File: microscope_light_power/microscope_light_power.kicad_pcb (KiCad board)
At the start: 2 copper layers, 50 x 40 mm, 36 parts, among them J1 MICROUSB, J2 5V175_out, J3 enable_switch, U1 MCP73871-2AA, U2 TPS61090

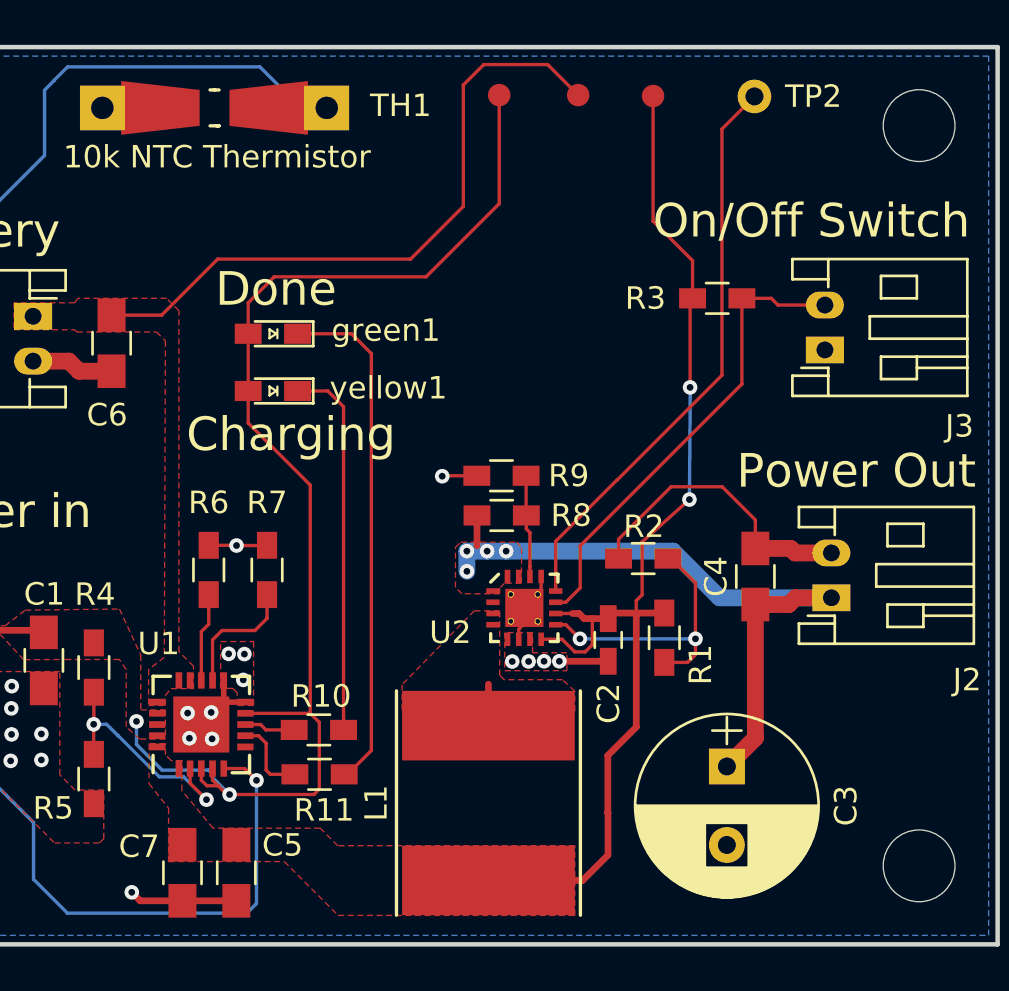
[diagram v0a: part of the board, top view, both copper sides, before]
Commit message: Add more silkscreen labels for clarity
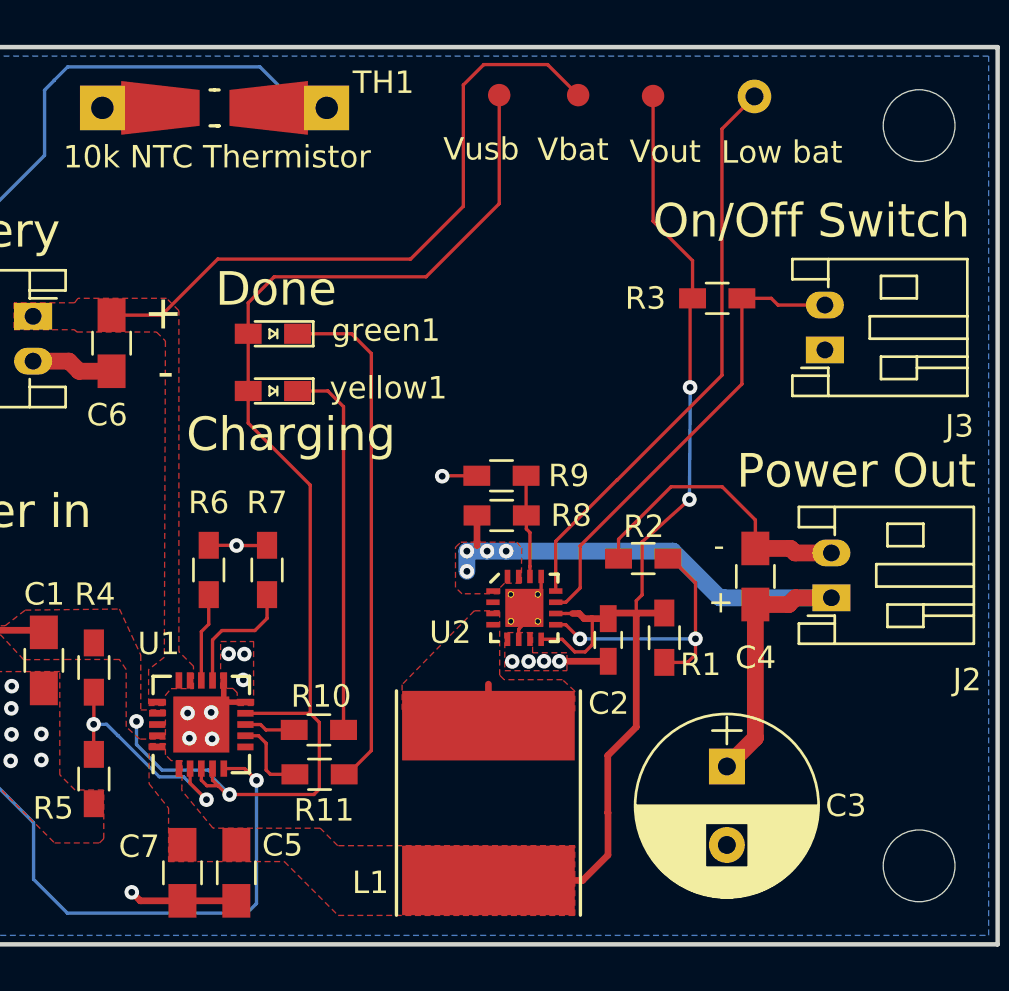
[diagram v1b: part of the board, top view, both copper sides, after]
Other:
- board text added: "+"
- board text added: "-"
- board text added: "5V@1.5A out"
- board text added: "Jon Neal"
- board text added: "Low bat"
- board text added: "USB battery charger with 5V out"
- board text added: "Vbat"
- board text added: "Vout"
- board text added: "Vusb"
- board text added: "github.com/reportingsjr/microscope_light_power"
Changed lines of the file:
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@@
 (general
   (thickness 1.6)
-  (drawings 15)
+  (drawings 27)
   (tracks 234)
   (zones 0)
@@
 (general
   (thickness 1.6)
-  (drawings 15)
+  (drawings 27)
   (tracks 234)
   (zones 0)
@@
     (tags "capacitor 0603")
     (attr smd)
-    (fp_text reference C2 (at 2.83 -0.02 270) (layer F.SilkS)
+    (fp_text reference C2 (at 2.83 -0.02) (layer F.SilkS)
       (effects (font (size 1 1) (thickness 0.15)))
     )
@@
     (fp_line (start 0.8 0.4) (end -0.8 0.4) (layer F.Fab) (width 0.1))
     (fp_line (start -0.8 0.4) (end -0.8 -0.4) (layer F.Fab) (width 0.1))
-    (fp_text user %R (at 2.83 -0.02 270) (layer F.Fab)
+    (fp_text user %R (at 2.83 -0.02) (layer F.Fab)
       (effects (font (size 1 1) (thickness 0.15)))
     )
@@
     (tags "capacitor 0805")
     (attr smd)
-    (fp_text reference C4 (at 0 -1.75 90) (layer F.SilkS)
+    (fp_text reference C4 (at -3.62 0.01) (layer F.SilkS)
       (effects (font (size 1 1) (thickness 0.15)))
     )
@@
       (effects (font (size 1 1) (thickness 0.15)))
     )
-    (fp_text user %R (at 0 -1.75 90) (layer F.Fab)
+    (fp_text user %R (at -3.62 0.01 180) (layer F.Fab)
       (effects (font (size 1 1) (thickness 0.15)))
     )
@@
     (descr "CP, Radial series, Radial, pin pitch=3.50mm, , diameter=8mm, Electrolytic Capacitor")
     (tags "CP Radial series Radial pin pitch 3.50mm  diameter 8mm Electrolytic Capacitor")
-    (fp_text reference C3 (at 1.75 -5.31 270) (layer F.SilkS)
+    (fp_text reference C3 (at 1.75 -5.31) (layer F.SilkS)
       (effects (font (size 1 1) (thickness 0.15)))
     )
@@
     (tags "inductor taiyo-yuden nr smd")
     (attr smd)
-    (fp_text reference L1 (at 0 -5 90) (layer F.SilkS)
+    (fp_text reference L1 (at -3.55 -5.26 180) (layer F.SilkS)
       (effects (font (size 1 1) (thickness 0.15)))
     )
@@
     (tags "Mesurement Point Round Trough Hole 1.5mm Drill 0.8mm")
     (attr virtual)
-    (fp_text reference TP2 (at 2.63 0) (layer F.SilkS)
+    (fp_text reference TP2 (at 2.63 0) (layer F.SilkS) hide
       (effects (font (size 1 1) (thickness 0.15)))
     )
@@
     (tags "resistor 0603")
     (attr smd)
-    (fp_text reference R1 (at 1.2 -1.62 270) (layer F.SilkS)
+    (fp_text reference R1 (at 1.2 -1.62) (layer F.SilkS)
       (effects (font (size 1 1) (thickness 0.15)))
     )
@@
     (descr "Resistor, SMD and THT, universal, 0805 to 1206,RM10,  Hand soldering,")
     (tags "Resistor, SMD and THT, universal, 0805 to 1206, RM10, Hand soldering,")
-    (fp_text reference TH1 (at -8.3 0.1 180) (layer F.SilkS)
+    (fp_text reference TH1 (at -7.53 1.13 180) (layer F.SilkS)
       (effects (font (size 1 1) (thickness 0.15)))
     )
@@
   (module agg:MICROUSB_MOLEX_47589-0001 (layer F.Cu)
     (at 101.5 147.3 270)
-    (fp_text reference J1 (at 5.8 0.6 270) (layer F.Fab)
+    (fp_text reference J1 (at 5.8 0.09) (layer F.Fab)
       (effects (font (size 1 1) (thickness 0.15)))
     )
@@
       (net 1 /Vbat))
   )
+  (gr_text "5V@1.5A out" (at 125.07 149.77) (layer B.SilkS)
+    (effects (font (size 1.5 1.5) (thickness 0.3)) (justify mirror))
+  )
+  (gr_text github.com/reportingsjr/microscope_light_power (at 125.32 140.32) (layer B.SilkS)
+    (effects (font (size 1.25 1.25) (thickness 0.3)) (justify mirror))
+  )
+  (gr_text "USB battery charger with 5V out" (at 126.55 136.51) (layer B.SilkS)
+    (effects (font (size 1.5 1.5) (thickness 0.3)) (justify mirror))
+  )
+  (gr_text "Jon Neal" (at 125.81 133.01) (layer B.SilkS)
+    (effects (font (size 1.5 1.5) (thickness 0.3)) (justify mirror))
+  )
+  (gr_text + (at 137.66 144.74) (layer F.SilkS)
+    (effects (font (size 1 1) (thickness 0.25)))
+  )
+  (gr_text - (at 137.58 142.23) (layer F.SilkS)
+    (effects (font (size 1 1) (thickness 0.25)))
+  )
+  (gr_text "Low bat" (at 140.38 124.69) (layer F.SilkS)
+    (effects (font (size 1 1) (thickness 0.25)))
+  )
+  (gr_text Vout (at 135.18 124.66) (layer F.SilkS)
+    (effects (font (size 1 1) (thickness 0.25)))
+  )
+  (gr_text Vbat (at 131.07 124.57) (layer F.SilkS)
+    (effects (font (size 1 1) (thickness 0.25)))
+  )
+  (gr_text Vusb (at 126.98 124.55) (layer F.SilkS)
+    (effects (font (size 1 1) (thickness 0.25)))
+  )
+  (gr_text - (at 112.91 134.48) (layer F.SilkS)
+    (effects (font (size 1.5 1.5) (thickness 0.3)))
+  )
+  (gr_text + (at 112.8 131.85) (layer F.SilkS)
+    (effects (font (size 1.5 1.5) (thickness 0.3)))
+  )
   (gr_line (start 104.6 149.53) (end 104.4 149.53) (layer Edge.Cuts) (width 0.65))

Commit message: Added OSHW symbol
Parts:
- added REF***: OSHW-Logo_7.5x8mm_SilkScreen, Symbols:OSHW-Logo_7.5x8mm_SilkScreen, B.Cu at (124.2, 155.0)

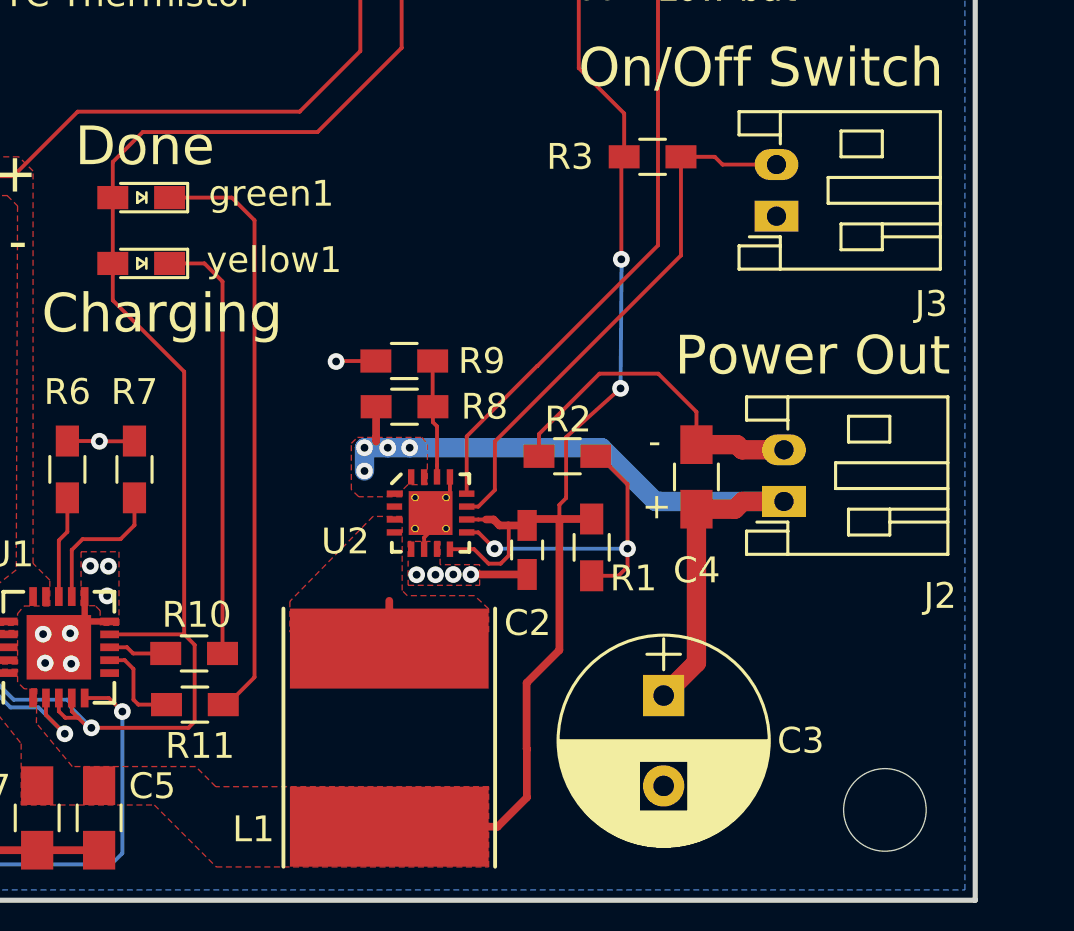
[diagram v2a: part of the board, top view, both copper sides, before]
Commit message: Updated TPS61090 footprint to the correct footprint and modified the symbol to match KLC. sym-lib-table is due to a recent change in KiCad.
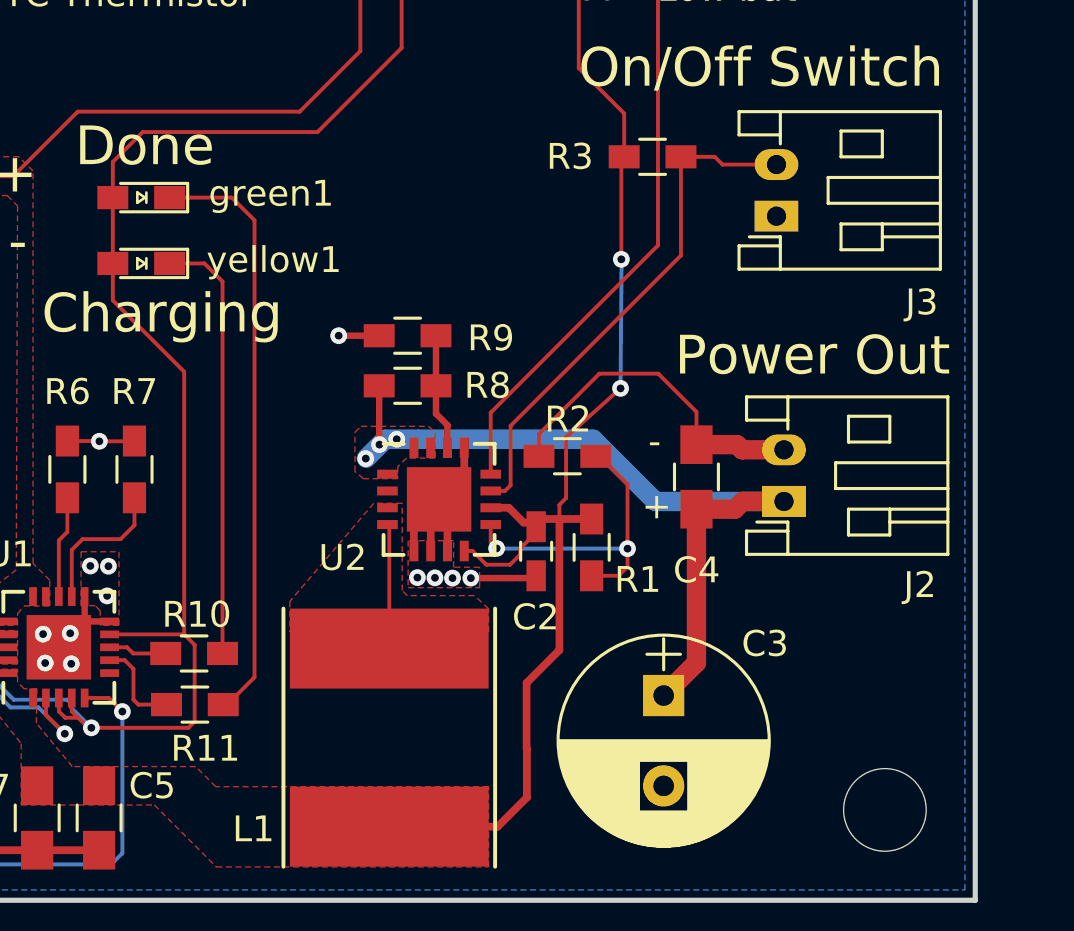
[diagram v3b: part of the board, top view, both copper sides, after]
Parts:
- removed REF***: OSHW-Logo_7.5x8mm_SilkScreen, Symbols:OSHW-Logo_7.5x8mm_SilkScreen
- U2: footprint agg:QFN-16-EP-TI -> Housings_DFN_QFN:QFN-16-1EP_4x4mm_Pitch0.65mm
- moved R9 0.99 mm to (128.0, 138.1)
- moved R8 0.82 mm to (128.0, 140.1)
- moved U2 0.62 mm to (129.2, 144.5)
- moved C2 0.35 mm to (133.0, 146.5)
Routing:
- net GND: track 35.5 -> 43.4 mm
- net /SW: track 1.85 -> 4.83 mm
- net /low_battery: track 25.7 -> 24.6 mm
- net /enable: track 21.1 -> 20.1 mm
- net /Vout: track 50.9 -> 50.2 mm
- net /5V175: track 30.6 -> 31.0 mm, vias 4 -> 3

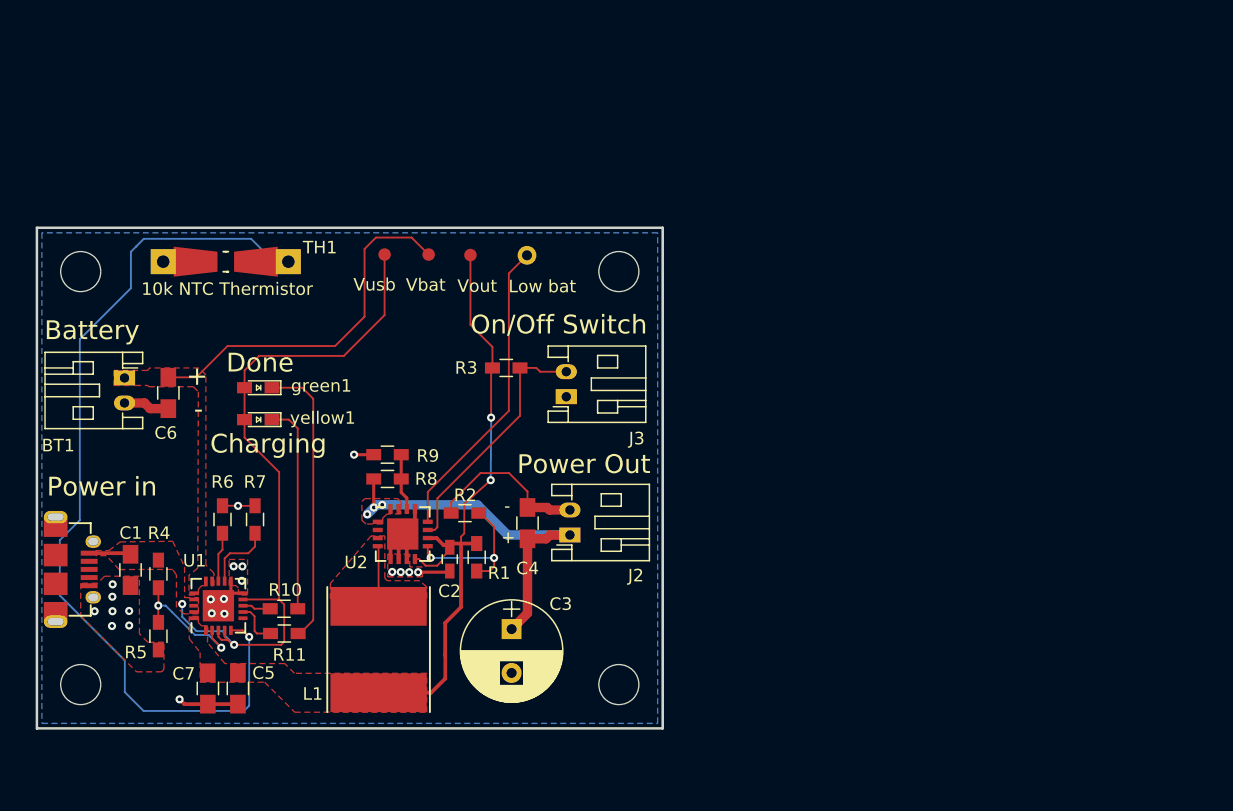
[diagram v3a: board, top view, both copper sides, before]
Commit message: Start redoing the layout to fix some major and minor problems with this design: * The SMPS output filter caps are way too far away from the IC. This   keeps killing the internal MOSFET which fails as a short to ground   causing rapid heating and will quickly kill the battery. * The connectors weren't in very good locations. * The PCB is quite a lot bigger than it needs to be. The next rev will   a fun experiment in minituarizing this PCB! * Switch from test pads to test /throughholes/ that are a reasonable   to solder to. * Will add a second pad so the On/Off switch can be switched to normally   on or normally off.
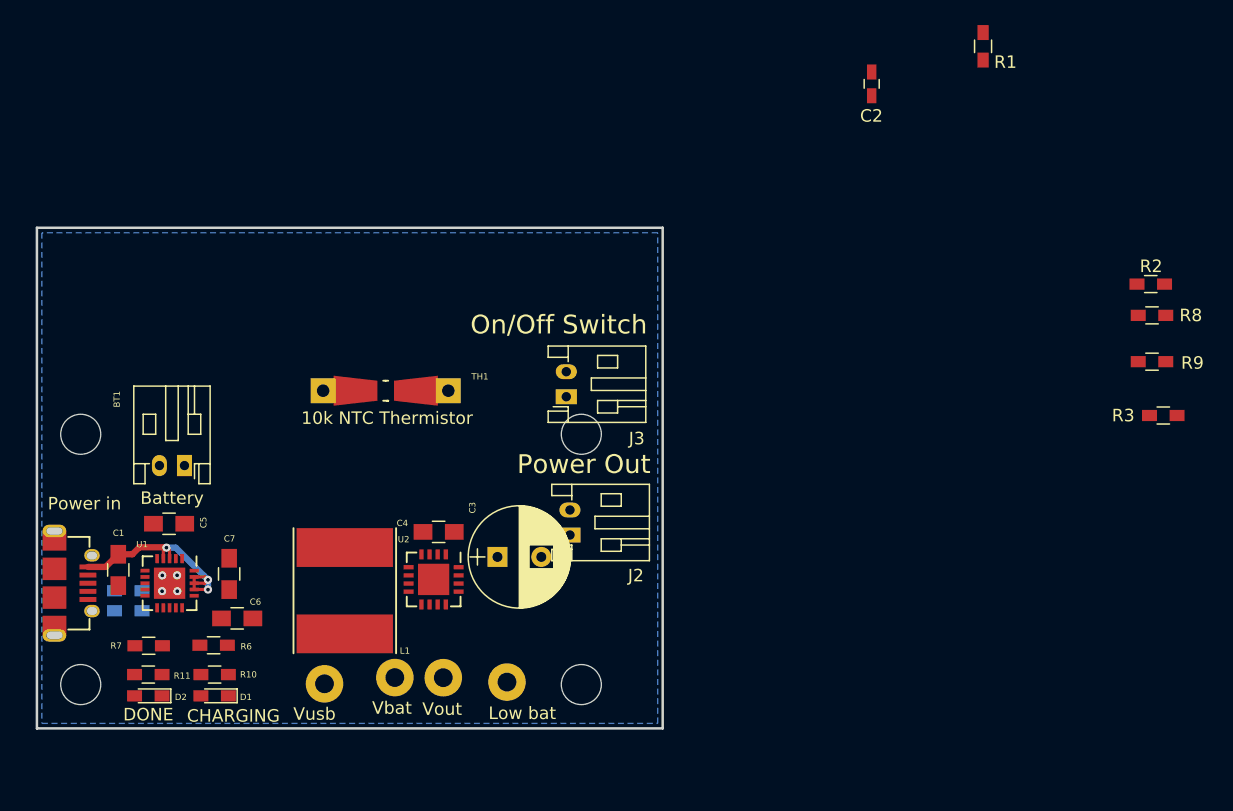
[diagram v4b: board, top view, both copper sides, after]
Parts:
- removed green1: done, LEDs:LED_0603_HandSoldering
- removed yellow1: charging, LEDs:LED_0603_HandSoldering
- added D1: charging, LEDs:LED_0603_HandSoldering, F.Cu at (114.2, 157.4)
- added D2: done, LEDs:LED_0603_HandSoldering, F.Cu at (108.9, 157.4)
- R4, R5: moved to B.Cu
- TP1, TP3, TP4: footprint agg:TESTPAD -> Measurement_Points:Measurement_Point_Round-TH_Big
- TP2: footprint Measurement_Points:Measurement_Point_Round-TH_Small -> Measurement_Points:Measurement_Point_Round-TH_Big
- moved R8 62.5 mm to (189.1, 127.0)
- moved R9 61.5 mm to (189.1, 130.7)
- moved R2 57.8 mm to (189.0, 124.5)
- moved R1 57.5 mm to (175.6, 105.5)
- moved R3 52.6 mm to (190.0, 135.0)
- moved C2 50.8 mm to (166.7, 108.5)
- moved TP1 34.6 mm to (123.0, 156.4)
- moved TP2 34.1 mm to (137.6, 156.3)
- moved TP3 33.9 mm to (128.6, 155.9)
- moved TP4 33.8 mm to (132.5, 155.9)
- moved C6 18.8 mm to (116.0, 151.2), turned to 0 degrees
- moved TH1 16.4 mm to (127.9, 133.0)
- moved C5 14.3 mm to (110.6, 143.7), turned to 180 degrees
- moved MK1 13.3 mm to (143.5, 136.5)
- moved R7 13.2 mm to (108.9, 153.4), turned to 180 degrees
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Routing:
- net Net-(TH1-Pad1): track 74.0 -> 0.00 mm, vias 1 -> 0
- net /Vout: track 50.2 -> 0.00 mm, vias 2 -> 0
- net GND: track 43.4 -> 0.00 mm, vias 21 -> 4
- net /Vusb: track 60.3 -> 18.7 mm, vias 2 -> 3
- net /5V175: track 31.0 -> 0.00 mm, vias 3 -> 0
- net /Vbat: track 29.2 -> 0.00 mm
- net /low_battery: track 24.6 -> 0.00 mm
- net Net-(D2-Pad1): track 23.0 -> 0.00 mm
- net /enable: track 20.1 -> 0.00 mm
- net Net-(D1-Pad1): track 16.7 -> 0.00 mm
- net Net-(R1-Pad2): track 12.5 -> 0.00 mm, vias 2 -> 0
- net Net-(R4-Pad1): track 10.9 -> 0.00 mm, vias 2 -> 0
- net Net-(R7-Pad1): track 5.69 -> 0.00 mm
- net /SW: track 4.83 -> 0.00 mm
- net Net-(R8-Pad2): track 4.52 -> 0.00 mm
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- removed copper zone on F.Cu, net /5V175
- removed copper zone on F.Cu, net /SW
- removed copper zone on F.Cu, net /Vbat
- removed copper zone on F.Cu, net /Vout
- removed copper zone on F.Cu, net /Vusb
- removed copper zone on F.Cu, net GND
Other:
- outline, holes or cut-outs redrawn
- board text added: "CHARGING"
- board text added: "DONE"
- board text removed: "+"
- board text removed: "-"
- board text removed: "5V@1.5A out"
- board text removed: "Charging"
- board text removed: "Done"
- board text removed: "Jon Neal"
- board text removed: "USB battery charger with 5V out"
- board text removed: "github.com/reportingsjr/microscope_light_power"
